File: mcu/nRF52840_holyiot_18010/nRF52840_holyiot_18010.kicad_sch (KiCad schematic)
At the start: 3 parts

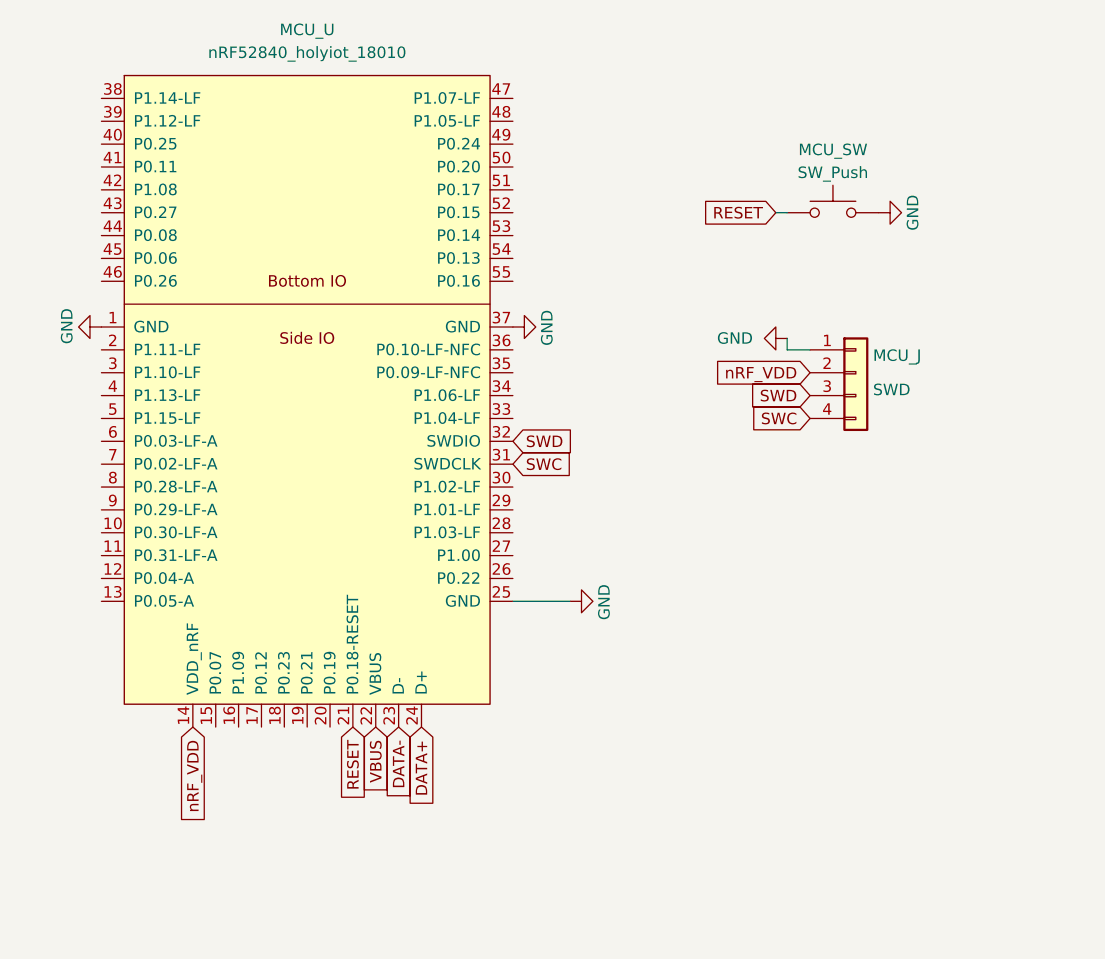
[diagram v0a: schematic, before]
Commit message: upgrade modules with kicad_sh and kicad_pcb
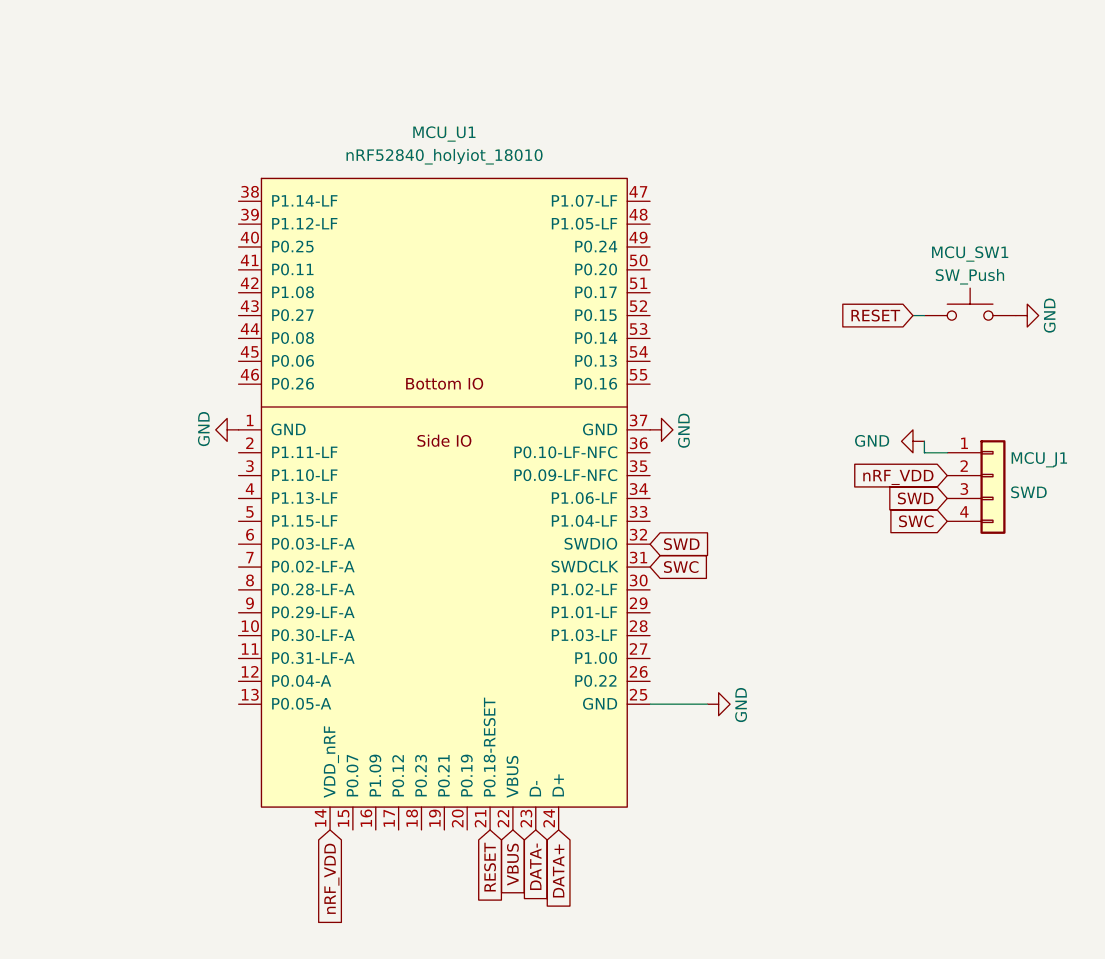
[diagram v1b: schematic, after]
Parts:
- renumbered MCU_J to MCU_J1, MCU_SW to MCU_SW1, MCU_U to MCU_U1
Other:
- moved on the sheet: MCU_J1, MCU_SW1, MCU_U1

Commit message: update battery module
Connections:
- net AnalogInput: now reaches MCU_U1.10 (P0.30-LF-A)
- net AnalogInput: now also MCU_U1.11 (P0.31-LF-A), MCU_U1.6 (P0.03-LF-A), MCU_U1.7 (P0.02-LF-A), MCU_U1.8 (P0.28-LF-A), MCU_U1.9 (P0.29-LF-A)
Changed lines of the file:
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@@
+		)
+	)
+	(global_label "AnalogInput"
+		(shape input)
+		(at 68.58 82.55 180)
+		(fields_autoplaced yes)
+		(effects
+			(font
+				(size 1.27 1.27)
+			)
+			(justify right)
+		)
+		(property "Intersheetrefs" "${INTERSHEET_REFS}"
+			(at 54.4675 82.55 0)
+			(effects
+				(font
+					(size 1.27 1.27)
+				)
+				(justify right)
+				(hide yes)
+			)
+		)
+	)
+	(global_label "AnalogInput"
+		(shape input)
+		(at 68.58 92.71 180)
+		(fields_autoplaced yes)
+		(effects
+			(font
+				(size 1.27 1.27)
+			)
+			(justify right)
+		)
+		(property "Intersheetrefs" "${INTERSHEET_REFS}"
+			(at 54.4675 92.71 0)
+			(effects
+				(font
+					(size 1.27 1.27)
+				)
+				(justify right)
+				(hide yes)
+			)
 		)
 	)
@@
 		)
 	)
+	(global_label "AnalogInput"
+		(shape input)
+		(at 68.58 90.17 180)
+		(fields_autoplaced yes)
+		(effects
+			(font
+				(size 1.27 1.27)
+			)
+			(justify right)
+		)
+		(property "Intersheetrefs" "${INTERSHEET_REFS}"
+			(at 54.4675 90.17 0)
+			(effects
+				(font
+					(size 1.27 1.27)
+				)
+				(justify right)
+				(hide yes)
+			)
+		)
+	)
+	(global_label "AnalogInput"
+		(shape input)
+		(at 68.58 80.01 180)
+		(fields_autoplaced yes)
+		(effects
+			(font
+				(size 1.27 1.27)
+			)
+			(justify right)
+		)
+		(property "Intersheetrefs" "${INTERSHEET_REFS}"
+			(at 54.4675 80.01 0)
+			(effects
+				(font
+					(size 1.27 1.27)
+				)
+				(justify right)
+				(hide yes)
+			)
+		)
+	)
 	(global_label "SWC"
 		(shape input)
@@
 				(hide yes)
 			)
+		)
+	)
+	(global_label "AnalogInput"
+		(shape input)
+		(at 68.58 85.09 180)
+		(fields_autoplaced yes)
+		(effects
+			(font
+				(size 1.27 1.27)
+			)
+			(justify right)
+		)
+		(property "Intersheetrefs" "${INTERSHEET_REFS}"
+			(at 54.4675 85.09 0)
+			(effects
+				(font
+					(size 1.27 1.27)
+				)
+				(justify right)
+				(hide yes)
+			)
+		)
+	)
+	(global_label "AnalogInput"
+		(shape input)
+		(at 68.58 87.63 180)
+		(fields_autoplaced yes)
+		(effects
+			(font
+				(size 1.27 1.27)
+			)
+			(justify right)
+		)
+		(property "Intersheetrefs" "${INTERSHEET_REFS}"
+			(at 54.4675 87.63 0)
+			(effects
+				(font
+					(size 1.27 1.27)
+				)
+				(justify right)
+				(hide yes)
+			)

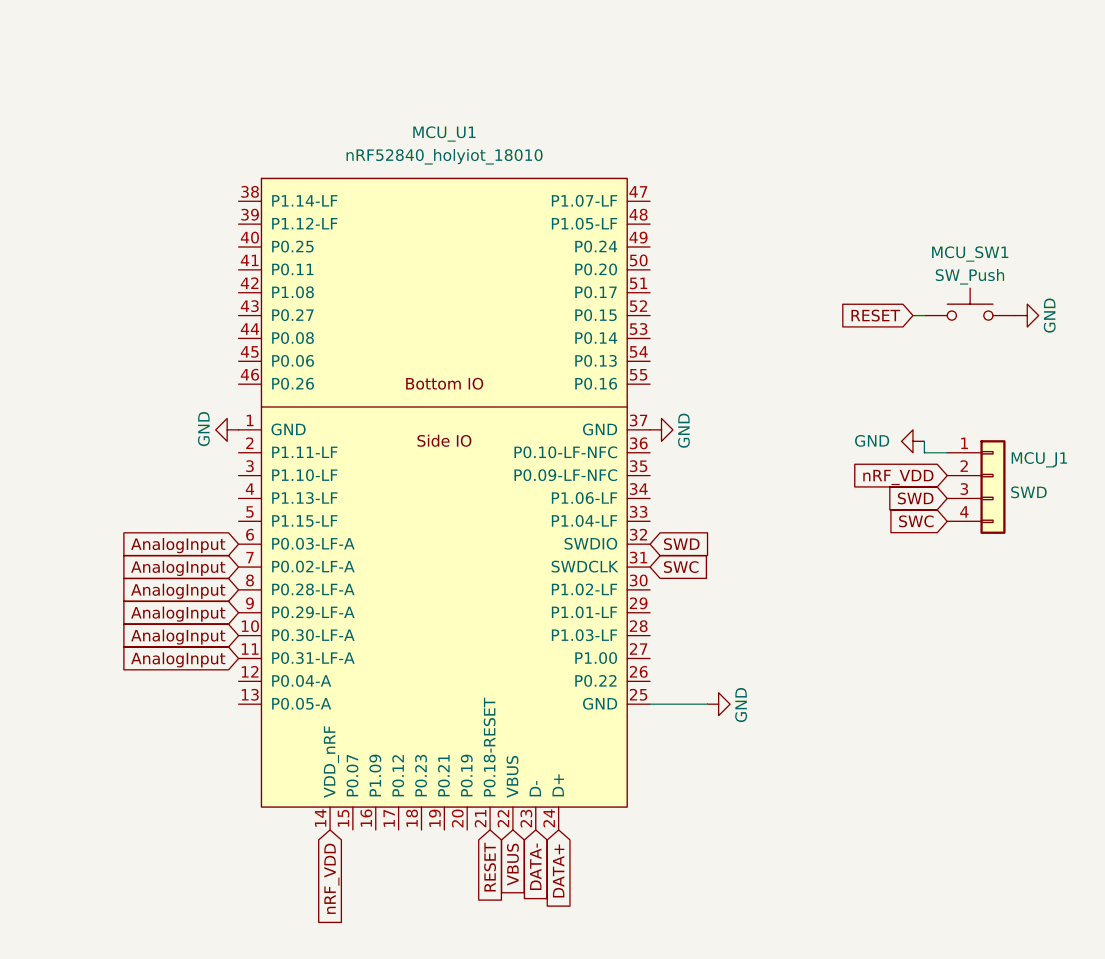
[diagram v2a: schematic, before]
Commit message: use nrf52840 simple
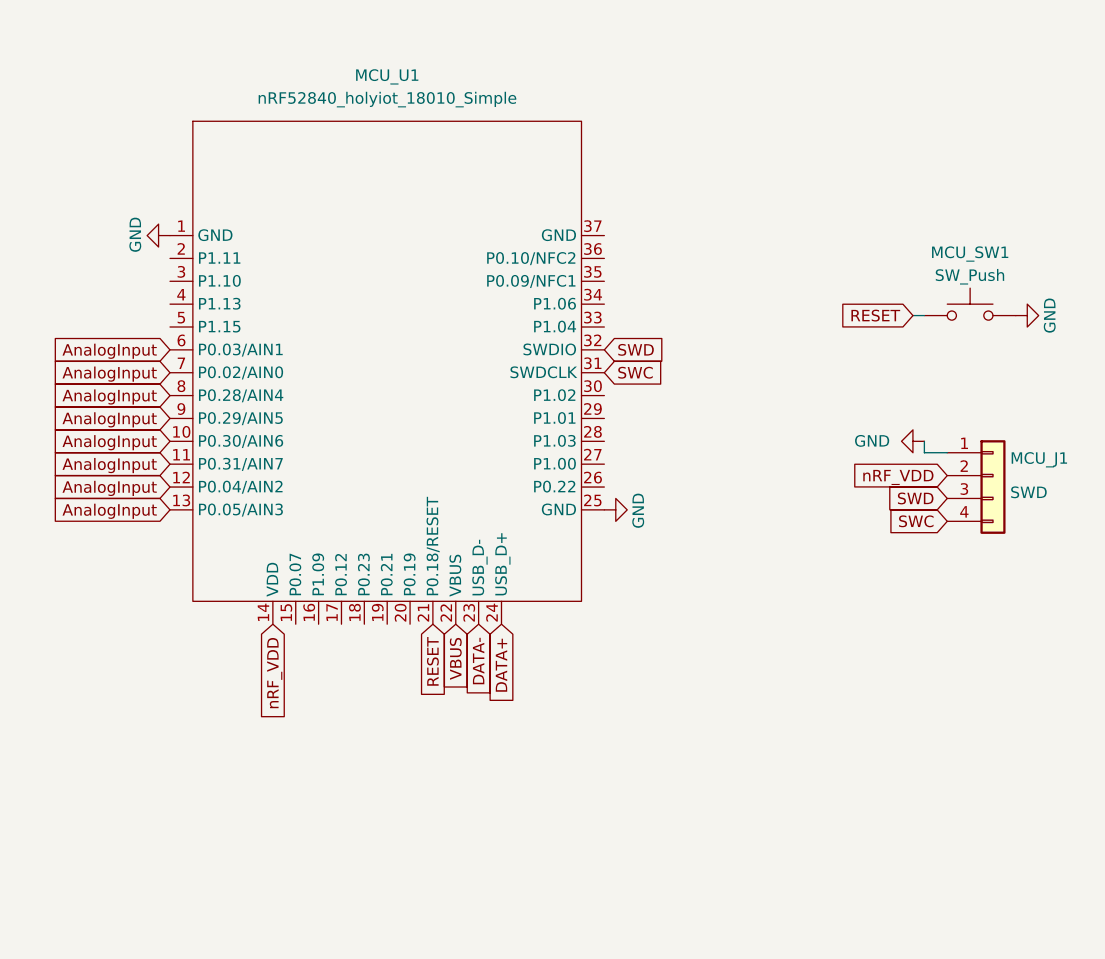
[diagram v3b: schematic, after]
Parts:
- removed MCU_U1: nRF52840_holyiot_18010, ErgoCai.pretty:nRF52840_holyiot_18010, symbol ErgoCai:nRF52840_holyiot_18010
- added MCU_U1: nRF52840_holyiot_18010_Simple, ErgoCai.pretty:nRF52840_holyiot_18010_HS_simple, symbol ErgoCai:nRF52840_holyiot_18010_Simple
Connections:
- net AnalogInput: now also MCU_U1.10 (P0.30/AIN6), MCU_U1.11 (P0.31/AIN7), MCU_U1.12 (P0.04/AIN2), MCU_U1.13 (P0.05/AIN3), MCU_U1.6 (P0.03/AIN1), MCU_U1.7 (P0.02/AIN0), MCU_U1.8 (P0.28/AIN4), MCU_U1.9 (P0.29/AIN5)
- net DATA+: now also MCU_U1.24 (USB_D+)
- net DATA-: now also MCU_U1.23 (USB_D-)
- net GND: now also MCU_U1.1 (GND), MCU_U1.25 (GND)
- net RESET: now also MCU_U1.21 (P0.18/RESET)
- net SWC: now also MCU_U1.31 (SWDCLK)
- net SWD: now also MCU_U1.32 (SWDIO)
- net VBUS: now also MCU_U1.22 (VBUS)
- net nRF_VDD: now also MCU_U1.14 (VDD)

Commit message: update battery module, change switch
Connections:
- net GND: now also MCU_U1.37 (GND)
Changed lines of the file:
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@@
+	)
+	(symbol
+		(lib_id "power:GND")
+		(at 109.22 45.72 90)
+		(unit 1)
+		(exclude_from_sim no)
+		(in_bom yes)
+		(on_board yes)
+		(dnp no)
+		(property "Reference" "#PWR03"
+			(at 115.57 45.72 0)
+			(effects
+				(font
+					(size 1.27 1.27)
+				)
+				(hide yes)
+			)
+		)
+		(property "Value" "GND"
+			(at 113.03 43.815 0)
+			(effects
+				(font
+					(size 1.27 1.27)
+				)
+				(justify right)
+			)
+		)
+		(property "Footprint" ""
+			(at 109.22 45.72 0)
+			(effects
+				(font
+					(size 1.27 1.27)
+				)
+				(hide yes)
+			)
+		)
+		(property "Datasheet" ""
+			(at 109.22 45.72 0)
+			(effects
+				(font
+					(size 1.27 1.27)
+				)
+				(hide yes)
+			)
+		)
+		(property "Description" "Power symbol creates a global label with name \"GND\" , ground"
+			(at 109.22 45.72 0)
+			(effects
+				(font
+					(size 1.27 1.27)
+				)
+				(hide yes)
+			)
+		)
+		(pin "1"
+		)
+		(instances
+			(project "nRF52840_holyiot_18010"
+				(path "/a75e1a70-312e-4b3d-9ad5-017ab62e82c1"
+					(reference "#PWR03")
+					(unit 1)
+				)
+			)
+		)
 	)
 	(symbol

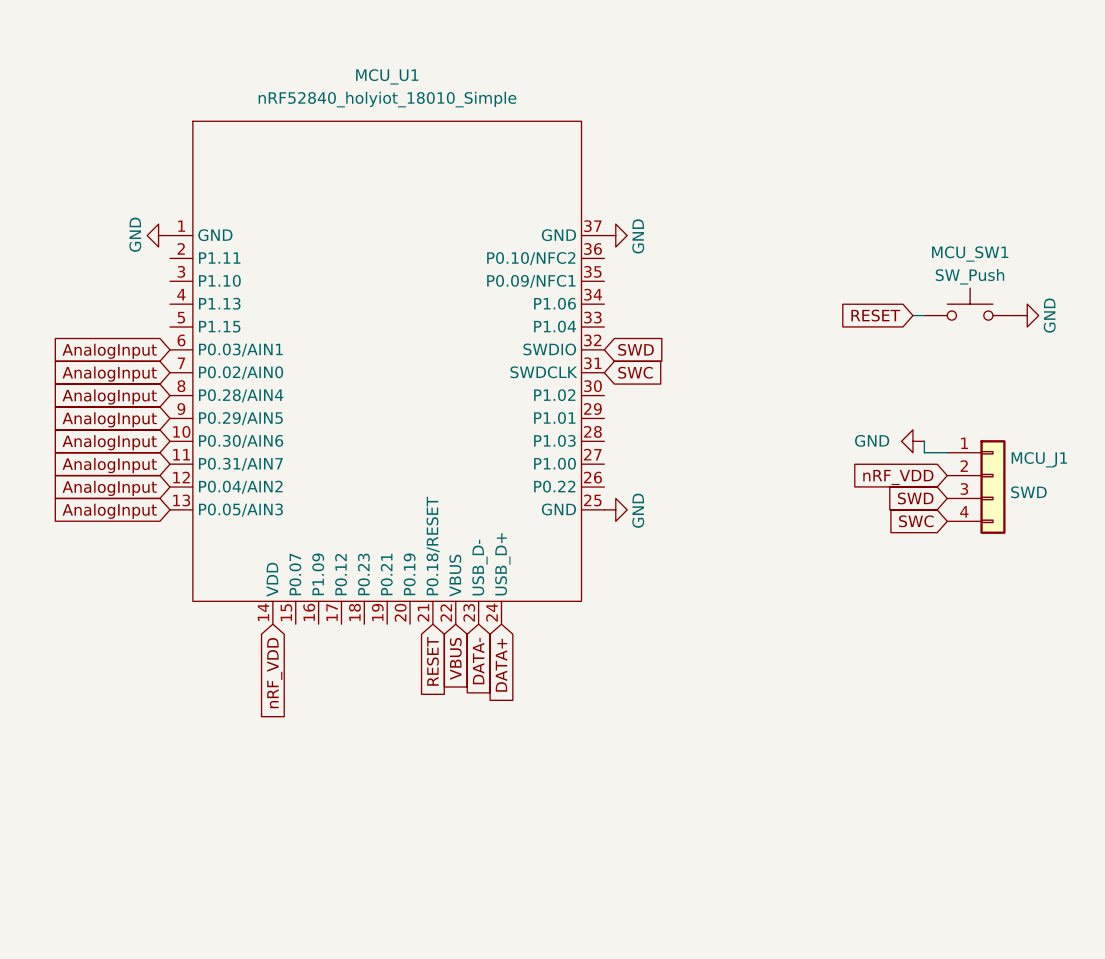
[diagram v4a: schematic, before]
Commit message: replace VDD-nRF to VCC
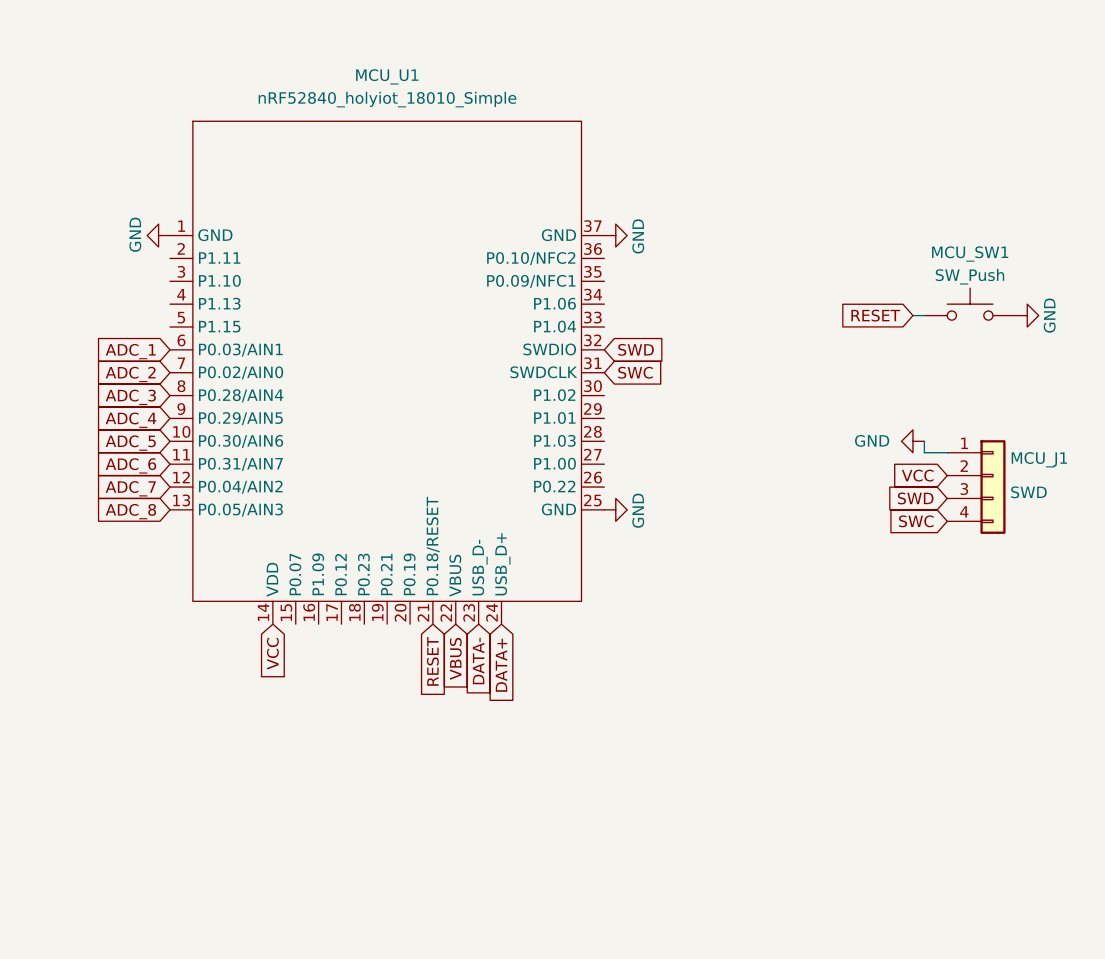
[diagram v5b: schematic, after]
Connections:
- removed net AnalogInput: MCU_U1.10 (P0.30/AIN6), MCU_U1.11 (P0.31/AIN7), MCU_U1.12 (P0.04/AIN2), MCU_U1.13 (P0.05/AIN3), MCU_U1.6 (P0.03/AIN1), MCU_U1.7 (P0.02/AIN0), MCU_U1.8 (P0.28/AIN4), MCU_U1.9 (P0.29/AIN5)
- net nRF_VDD renamed VCC
- new net ADC_1: MCU_U1.6 (P0.03/AIN1)
- new net ADC_2: MCU_U1.7 (P0.02/AIN0)
- new net ADC_3: MCU_U1.8 (P0.28/AIN4)
- new net ADC_4: MCU_U1.9 (P0.29/AIN5)
- new net ADC_5: MCU_U1.10 (P0.30/AIN6)
- new net ADC_6: MCU_U1.11 (P0.31/AIN7)
- new net ADC_7: MCU_U1.12 (P0.04/AIN2)
- new net ADC_8: MCU_U1.13 (P0.05/AIN3)
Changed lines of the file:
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@@
 		)
 	)
-	(global_label "nRF_VDD"
+	(global_label "VCC"
 		(shape input)
 		(at 147.32 72.39 180)
@@
 		)
 		(property "Intersheetrefs" "${INTERSHEET_REFS}"
-			(at 136.231 72.39 0)
-			(effects
-				(font
-					(size 1.27 1.27)
-				)
-				(justify right)
-				(hide yes)
-			)
-		)
-	)
-	(global_label "AnalogInput"
+			(at 140.7062 72.39 0)
+			(effects
+				(font
+					(size 1.27 1.27)
+				)
+				(justify right)
+				(hide yes)
+			)
+		)
+	)
+	(global_label "ADC_7"
 		(shape input)
 		(at 60.96 73.66 180)
@@
 		)
 		(property "Intersheetrefs" "${INTERSHEET_REFS}"
-			(at 46.8475 73.66 0)
+			(at 52.1691 73.66 0)
 			(effects
 				(font
@@
 		)
 	)
-	(global_label "AnalogInput"
+	(global_label "ADC_2"
 		(shape input)
 		(at 60.96 60.96 180)
@@
 		)
 		(property "Intersheetrefs" "${INTERSHEET_REFS}"
-			(at 46.8475 60.96 0)
+			(at 52.1691 60.96 0)
 			(effects
 				(font
@@
 		)
 	)
-	(global_label "AnalogInput"
+	(global_label "ADC_1"
 		(shape input)
 		(at 60.96 58.42 180)
@@
 		)
 		(property "Intersheetrefs" "${INTERSHEET_REFS}"
-			(at 46.8475 58.42 0)
-			(effects
-				(font
-					(size 1.27 1.27)
-				)
-				(justify right)
-				(hide yes)
-			)
-		)
-	)
-	(global_label "nRF_VDD"
+			(at 52.1691 58.42 0)
+			(effects
+				(font
+					(size 1.27 1.27)
+				)
+				(justify right)
+				(hide yes)
+			)
+		)
+	)
+	(global_label "VCC"
 		(shape input)
 		(at 72.39 88.9 270)
@@
 		)
 		(property "Intersheetrefs" "${INTERSHEET_REFS}"
-			(at 72.39 99.989 90)
-			(effects
-				(font
-					(size 1.27 1.27)
-				)
-				(justify right)
-				(hide yes)
-			)
-		)
-	)
-	(global_label "AnalogInput"
+			(at 72.39 95.5138 90)
+			(effects
+				(font
+					(size 1.27 1.27)
+				)
+				(justify right)
+				(hide yes)
+			)
+		)
+	)
+	(global_label "ADC_6"
 		(shape input)
 		(at 60.96 71.12 180)
@@
 		)
 		(property "Intersheetrefs" "${INTERSHEET_REFS}"
-			(at 46.8475 71.12 0)
+			(at 52.1691 71.12 0)
 			(effects
 				(font
@@
 		)
 	)
-	(global_label "AnalogInput"
+	(global_label "ADC_8"
 		(shape input)
 		(at 60.96 76.2 180)
@@
 		)
 		(property "Intersheetrefs" "${INTERSHEET_REFS}"
-			(at 46.8475 76.2 0)
-			(effects
-				(font
-					(size 1.27 1.27)
-				)
-				(justify right)
-				(hide yes)
-			)
-		)
-	)
-	(global_label "AnalogInput"
+			(at 52.1691 76.2 0)
+			(effects
+				(font
+					(size 1.27 1.27)
+				)
+				(justify right)
+				(hide yes)
+			)
+		)
+	)
+	(global_label "ADC_4"
 		(shape input)
 		(at 60.96 66.04 180)
@@
 		)
 		(property "Intersheetrefs" "${INTERSHEET_REFS}"
-			(at 46.8475 66.04 0)
+			(at 52.1691 66.04 0)
 			(effects
 				(font
@@
 		)
 	)
-	(global_label "AnalogInput"
+	(global_label "ADC_3"
 		(shape input)
 		(at 60.96 63.5 180)
@@
 		)
 		(property "Intersheetrefs" "${INTERSHEET_REFS}"
-			(at 46.8475 63.5 0)
-			(effects
-				(font
-					(size 1.27 1.27)
-				)
-				(justify right)
-				(hide yes)
-			)
-		)
-	)
-	(global_label "AnalogInput"
+			(at 52.1691 63.5 0)
+			(effects
+				(font
+					(size 1.27 1.27)
+				)
+				(justify right)
+				(hide yes)
+			)
+		)
+	)
+	(global_label "ADC_5"
 		(shape input)
 		(at 60.96 68.58 180)
@@
 		)
 		(property "Intersheetrefs" "${INTERSHEET_REFS}"
-			(at 46.8475 68.58 0)
-			(effects
-				(font
+			(at 52.1691 68.58 0)
+			(effects
+				(font
